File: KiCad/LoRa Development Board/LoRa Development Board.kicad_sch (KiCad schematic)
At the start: 0 parts

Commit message: Added SX1262 Symbol
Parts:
- added U1: ~, symbol Wireless Sensors:SX1262
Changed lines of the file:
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@@
     (company "NSE Labs")
+  )
+  (symbol (lib_id "Wireless Sensors:SX1262") (at 134.62 90.17 0) (unit 1)
+    (in_bom yes) (on_board yes) (dnp no) (fields_autoplaced)
+    (property "Reference" "U1" (at 137.8459 113.03 0)
+      (effects (font (size 1.27 1.27)) (justify left))
+    )
+    (property "Value" "~" (at 134.62 90.17 0)
+      (effects (font (size 1.27 1.27)))
+    )
+    (property "Footprint" "" (at 134.62 90.17 0)
+      (effects (font (size 1.27 1.27)) hide)
+    )
+    (property "Datasheet" "" (at 134.62 90.17 0)
+      (effects (font (size 1.27 1.27)) hide)
+    )
+    (pin "1")
+    (pin "10")
+    (pin "11")
+    (pin "12")
+    (pin "13")
+    (pin "14")
+    (pin "15")
+    (pin "16")
+    (pin "17")
+    (pin "18")
+    (pin "19")
+    (pin "2")
+    (pin "20")
+    (pin "21")
+    (pin "22")
+    (pin "23")
+    (pin "24")
+    (pin "3")
+    (pin "4")
+    (pin "5")
+    (pin "6")
+    (pin "7")
+    (pin "8")
+    (pin "9")
+    (instances
+      (project "LoRa Development Board"
+        (path "/81d1aadf-85d2-4fd0-839e-05ac66879581"
+          (reference "U1") (unit 1)
+        )
+      )
+    )
   )
   (sheet_instances

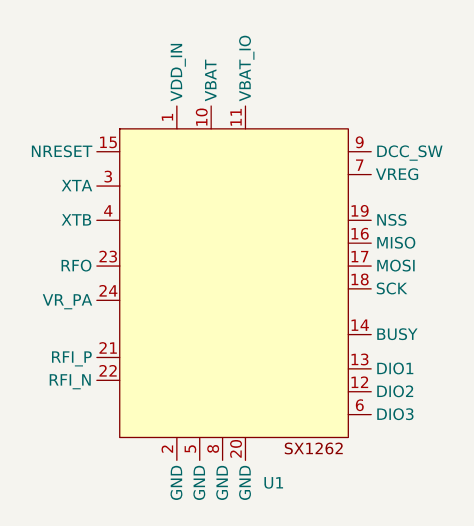
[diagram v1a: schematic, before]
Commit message: Update SX1262 Symbol
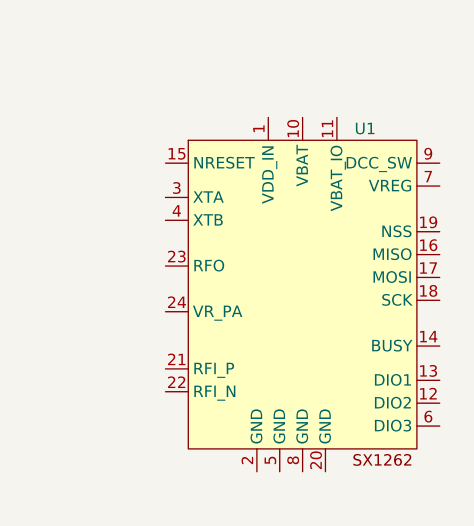
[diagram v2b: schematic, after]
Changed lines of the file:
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@@
     (company "NSE Labs")
   )
-  (symbol (lib_id "Wireless Sensors:SX1262") (at 134.62 90.17 0) (unit 1)
+  (symbol (lib_id "Wireless Sensors:SX1262") (at 142.24 91.44 0) (unit 1)
     (in_bom yes) (on_board yes) (dnp no) (fields_autoplaced)
-    (property "Reference" "U1" (at 137.8459 113.03 0)
+    (property "Reference" "U1" (at 148.0059 73.66 0)
       (effects (font (size 1.27 1.27)) (justify left))
     )
-    (property "Value" "~" (at 134.62 90.17 0)
+    (property "Value" "~" (at 142.24 91.44 0)
       (effects (font (size 1.27 1.27)))
     )
-    (property "Footprint" "" (at 134.62 90.17 0)
+    (property "Footprint" "" (at 142.24 91.44 0)
       (effects (font (size 1.27 1.27)) hide)
     )
-    (property "Datasheet" "" (at 134.62 90.17 0)
+    (property "Datasheet" "" (at 142.24 91.44 0)
       (effects (font (size 1.27 1.27)) hide)
     )

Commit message: Update LoRa Board Schematic
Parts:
- added C16: 1 uF, symbol Device:C_Small
- added C17: 470 nF, symbol Device:C_Small
- added C18: 100 nF, symbol Device:C_Small
- added L7: 15 uH, symbol Device:L_Small
- added Y1: 32.0 MHz, symbol Device:Crystal_GND24_Small
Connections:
- net +3.3V: now reaches U1.1 (VDD_IN)
- net +3.3V: now also U1.10 (VBAT), U1.11 (VBAT_IO), C16.2, C18.1
- net GND: now reaches U1.2 (GND)
- net GND: now also U1.20 (GND), U1.25 (GND), U1.5 (GND), U1.8 (GND), C16.1, C17.2, C18.2, Y1.2, Y1.4
- net at U1.3 (XTA): now also Y1.3
- net at U1.4 (XTB): now also Y1.1
- net at U1.7 (VREG): now also C17.1, L7.2
- net at U1.9 (DCC_SW): now also L7.1

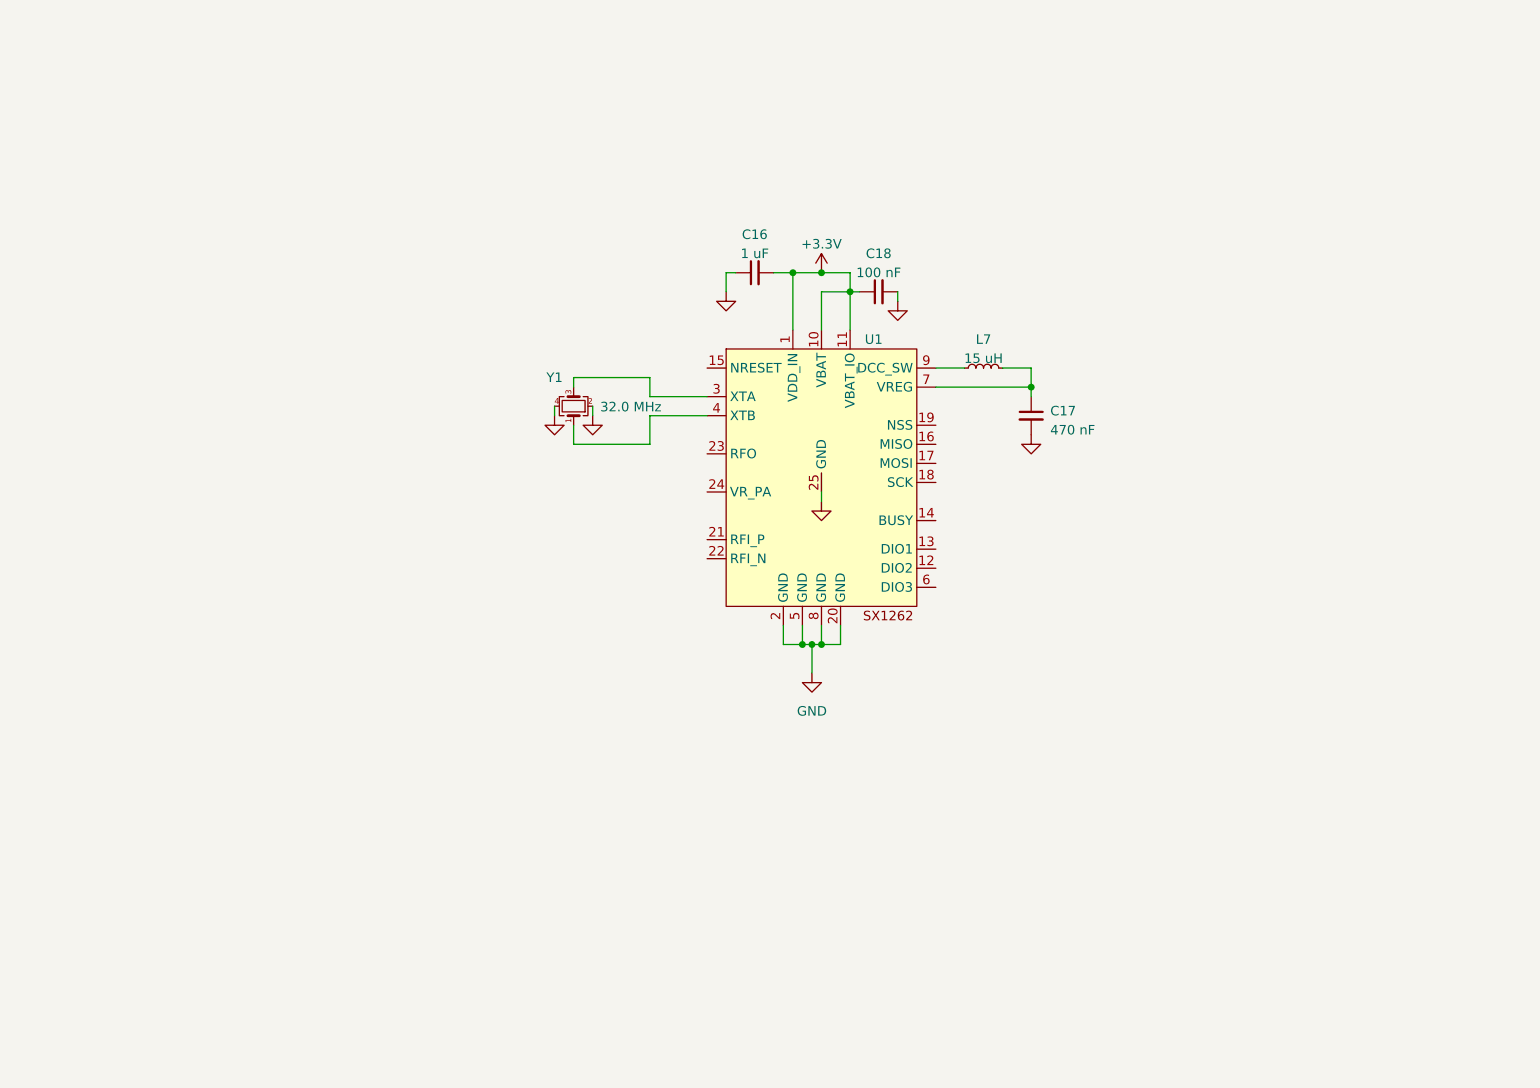
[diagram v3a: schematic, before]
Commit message: Completed schematic for LoRa board
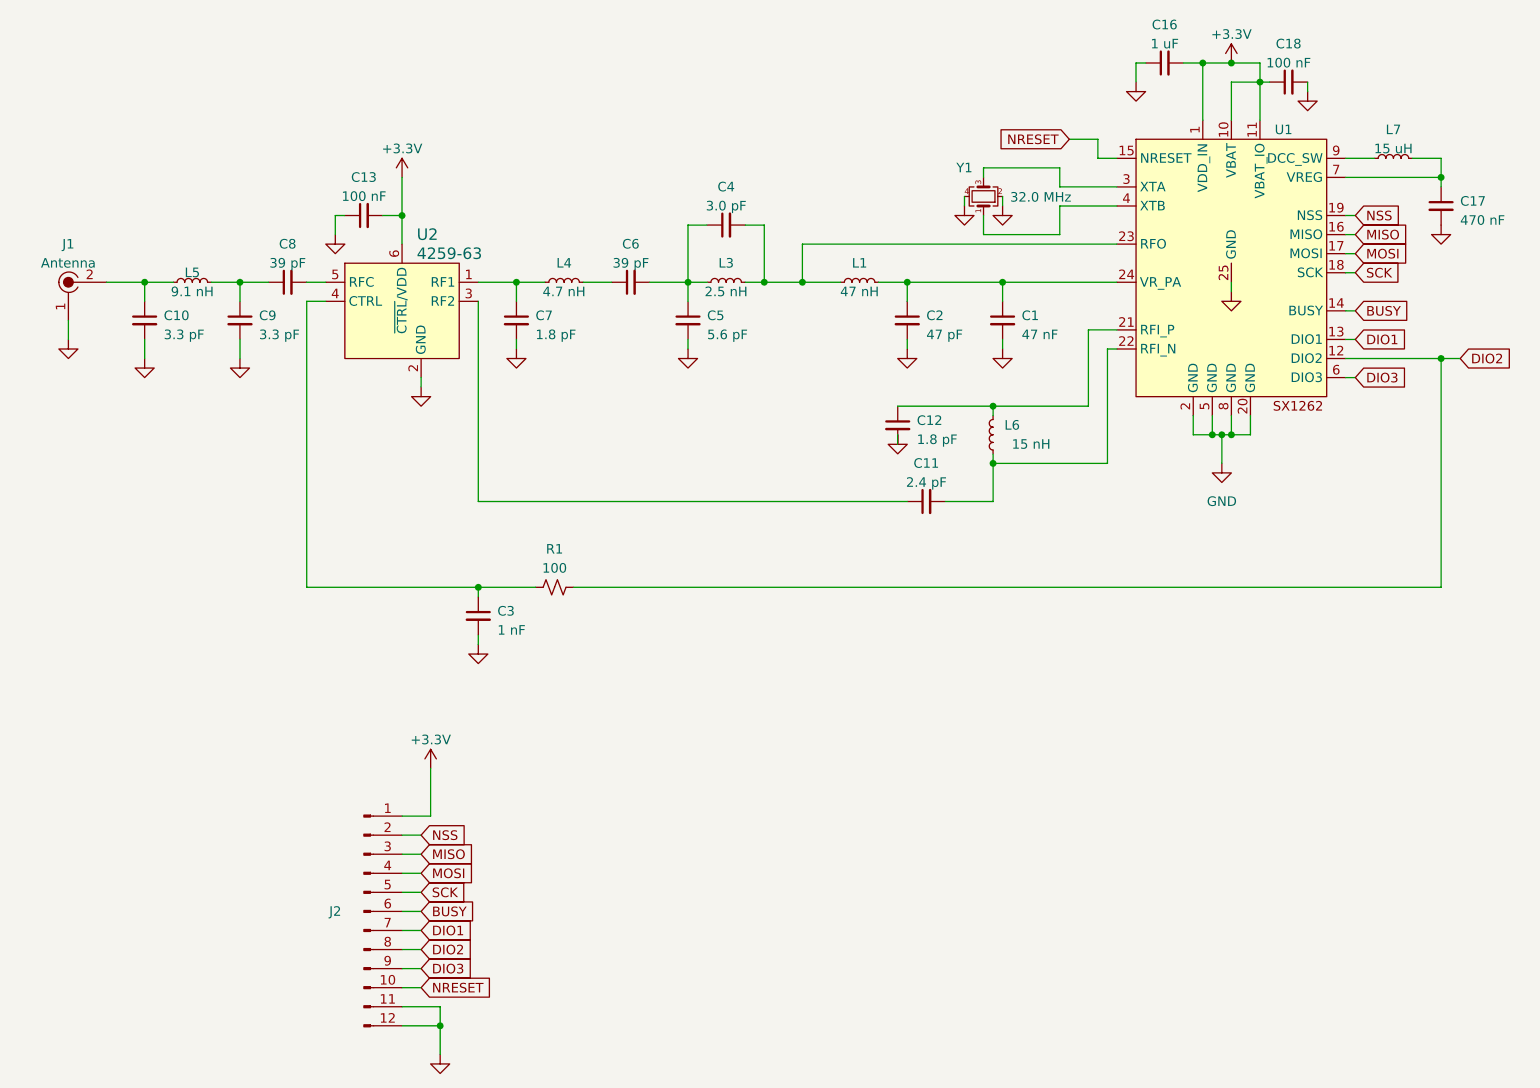
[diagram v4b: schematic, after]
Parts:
- added C1: 47 nF, symbol Device:C_Small
- added C10, C9: 3.3 pF, symbol Device:C_Small
- added C11: 2.4 pF, symbol Device:C_Small
- added C12, C7: 1.8 pF, symbol Device:C_Small
- added C13: 100 nF, symbol Device:C_Small
- added C2: 47 pF, symbol Device:C_Small
- added C3: 1 nF, symbol Device:C_Small
- added C4: 3.0 pF, symbol Device:C_Small
- added C5: 5.6 pF, symbol Device:C_Small
- added C6, C8: 39 pF, symbol Device:C_Small
- added J1: Antenna, digikey-footprints:Coax_Conn_U.FL, symbol dk_Coaxial-Connectors-RF:U_FL-R-SMT_10_
- added J2: ~, symbol Connector:Conn_01x12_Pin
- added L1: 47 nH, symbol Device:L_Small
- added L3: 2.5 nH, symbol Device:L_Small
- added L4: 4.7 nH, symbol Device:L_Small
- added L5: 9.1 nH, symbol Device:L_Small
- added L6: 15 nH, symbol Device:L_Small
- added R1: 100, symbol Device:R_Small_US
- added U2: 4259-63, digikey-footprints:SOT-363, symbol dk_RF-Switches:4259-63
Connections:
- net +3.3V: now also C13.2, J2.1 (Pin_1), U2.6 (~{CTRL}/VDD)
- net GND: now also C1.2, C10.2, C12.2, C13.1, C2.2, C3.2, C5.2, C7.2, C9.2, J1.1, J2.11 (Pin_11), J2.12 (Pin_12), U2.2 (GND)
- net DIO2: now reaches U1.12 (DIO2)
- net DIO2: now also J2.8 (Pin_8), R1.2
- net DIO1: now reaches U1.13 (DIO1)
- net DIO1: now also J2.7 (Pin_7)
- net BUSY: now reaches U1.14 (BUSY)
- net BUSY: now also J2.6 (Pin_6)
- net NRESET: now reaches U1.15 (NRESET)
- net NRESET: now also J2.10 (Pin_10)
- net MISO: now reaches U1.16 (MISO)
- net MISO: now also J2.3 (Pin_3)
- net MOSI: now reaches U1.17 (MOSI)
- net MOSI: now also J2.4 (Pin_4)
- net SCK: now reaches U1.18 (SCK)
- net SCK: now also J2.5 (Pin_5)
- net NSS: now reaches U1.19 (NSS)
- net NSS: now also J2.2 (Pin_2)
- net at U1.21 (RFI_P): now also C12.1, L6.2
- net at U1.22 (RFI_N): now also C11.2, L6.1
- net at U1.23 (RFO): now also C4.2, L1.1, L3.2
- net at U1.24 (VR_PA): now also C1.1, C2.1, L1.2
- net DIO3: now reaches U1.6 (DIO3)
- net DIO3: now also J2.9 (Pin_9)
- new net: C4.1, C5.1, C6.2, L3.1
- new net: C10.1, J1.2, L5.1
- new net: C8.1, C9.1, L5.2
- new net: C7.1, L4.1, U2.1 (RF1)
- new net: C11.1, U2.3 (RF2)
- new net: C6.1, L4.2
- new net: C3.1, R1.1, U2.4 (CTRL)
- new net: C8.2, U2.5 (RFC)
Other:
- moved on the sheet: C16, C17, C18, L7, U1, Y1

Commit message: Completed design and BOM
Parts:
- added R2: 100, symbol Device:R_Small_US
- C13: value 100 nF -> 1 nF
- renumbered C16 to C14, C18 to C15, C17 to C16
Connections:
- net +3.3V: no longer C13.2, U2.6 (~{CTRL}/VDD)
- net GND: no longer J2.11 (Pin_11)
- new net: C13.2, R2.1, U2.6 (~{CTRL}/VDD)
- new net ANT_SW: J2.11 (Pin_11), R2.2
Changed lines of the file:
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@@
   (title_block
     (title "LoRa Development Board")
-    (date "2023-05-02")
+    (date "2023-05-03")
     (rev "1")
     (company "NSE Labs")
@@
   (junction (at 96.52 106.68) (diameter 0) (color 0 0 0 0)
   )
-  (junction (at 91.44 165.1) (diameter 0) (color 0 0 0 0)
-  )
   (junction (at 194.31 86.36) (diameter 0) (color 0 0 0 0)
   )
@@
     (stroke (width 0) (type default))
   )
-  (wire (pts (xy 86.36 162.56) (xy 91.44 162.56))
-    (stroke (width 0) (type default))
-  )
   (wire (pts (xy 86.36 144.78) (xy 88.9 144.78))
     (stroke (width 0) (type default))
@@
     (stroke (width 0) (type default))
   )
-  (wire (pts (xy 86.36 52.07) (xy 86.36 57.15))
+  (wire (pts (xy 86.36 46.99) (xy 86.36 57.15))
     (stroke (width 0) (type default))
   )
@@
     (stroke (width 0) (type default))
   )
+  (wire (pts (xy 96.52 46.99) (xy 101.6 46.99))
+    (stroke (width 0) (type default))
+  )
   (wire (pts (xy 227.33 76.2) (xy 224.79 76.2))
     (stroke (width 0) (type default))
@@
     (stroke (width 0) (type default))
   )
+  (wire (pts (xy 86.36 162.56) (xy 88.9 162.56))
+    (stroke (width 0) (type default))
+  )
   (wire (pts (xy 200.66 39.37) (xy 201.93 39.37))
     (stroke (width 0) (type default))
@@
     (stroke (width 0) (type default))
   )
+  (wire (pts (xy 91.44 46.99) (xy 86.36 46.99))
+    (stroke (width 0) (type default))
+  )
   (wire (pts (xy 64.77 73.66) (xy 64.77 76.2))
     (stroke (width 0) (type default))
@@
   )
   (wire (pts (xy 181.61 74.93) (xy 180.34 74.93))
-    (stroke (width 0) (type default))
-  )
-  (wire (pts (xy 91.44 162.56) (xy 91.44 165.1))
     (stroke (width 0) (type default))
   )
@@
     )
   )
+  (global_label "ANT_SW" (shape input) (at 88.9 162.56 0) (fields_autoplaced)
+    (effects (font (size 1.27 1.27)) (justify left))
+    (property "Intersheetrefs" "${INTERSHEET_REFS}" (at 98.821 162.56 0)
+      (effects (font (size 1.27 1.27)) (justify left) hide)
+    )
+  )
   (global_label "BUSY" (shape input) (at 88.9 149.86 0) (fields_autoplaced)
     (effects (font (size 1.27 1.27)) (justify left))
@@
     )
   )
+  (global_label "ANT_SW" (shape input) (at 101.6 46.99 0) (fields_autoplaced)
+    (effects (font (size 1.27 1.27)) (justify left))
+    (property "Intersheetrefs" "${INTERSHEET_REFS}" (at 111.521 46.99 0)
+      (effects (font (size 1.27 1.27)) (justify left) hide)
+    )
+  )
   (global_label "DIO2" (shape input) (at 88.9 154.94 0) (fields_autoplaced)
     (effects (font (size 1.27 1.27)) (justify left))
@@
   (symbol (lib_id "Device:C_Small") (at 204.47 39.37 90) (unit 1)
     (in_bom yes) (on_board yes) (dnp no) (fields_autoplaced)
-    (property "Reference" "C18" (at 204.4763 34.29 90)
+    (property "Reference" "C15" (at 204.4763 34.29 90)
       (effects (font (size 1.27 1.27)))
     )
@@
       (project "LoRa Development Board"
         (path "/81d1aadf-85d2-4fd0-839e-05ac66879581"
-          (reference "C18") (unit 1)
+          (reference "C15") (unit 1)
         )
       )
@@
         (path "/81d1aadf-85d2-4fd0-839e-05ac66879581"
           (reference "#PWR01") (unit 1)
-        )
-      )
-    )
-  )
-  (symbol (lib_id "power:+3.3V") (at 86.36 52.07 0) (unit 1)
-    (in_bom yes) (on_board yes) (dnp no) (fields_autoplaced)
-    (property "Reference" "#PWR019" (at 86.36 55.88 0)
-      (effects (font (size 1.27 1.27)) hide)
-    )
-    (property "Value" "+3.3V" (at 86.36 48.26 0)
-      (effects (font (size 1.27 1.27)))
-    )
-    (property "Footprint" "" (at 86.36 52.07 0)
-      (effects (font (size 1.27 1.27)) hide)
-    )
-    (property "Datasheet" "" (at 86.36 52.07 0)
-      (effects (font (size 1.27 1.27)) hide)
-    )
-    (pin "1")
-    (instances
-      (project "LoRa Development Board"
-        (path "/81d1aadf-85d2-4fd0-839e-05ac66879581"
-          (reference "#PWR019") (unit 1)
         )
       )
@@
       (effects (font (size 1.27 1.27)))
     )
-    (property "Value" "100 nF" (at 81.2863 54.61 90)
+    (property "Value" "1 nF" (at 81.2863 54.61 90)
       (effects (font (size 1.27 1.27)))
     )
@@
     )
   )
+  (symbol (lib_id "Device:R_Small_US") (at 93.98 46.99 90) (unit 1)
+    (in_bom yes) (on_board yes) (dnp no) (fields_autoplaced)
+    (property "Reference" "R2" (at 93.98 41.91 90)
+      (effects (font (size 1.27 1.27)))
+    )
+    (property "Value" "100" (at 93.98 44.45 90)
+      (effects (font (size 1.27 1.27)))
+    )
+    (property "Footprint" "" (at 93.98 46.99 0)
+      (effects (font (size 1.27 1.27)) hide)
+    )
+    (property "Datasheet" "~" (at 93.98 46.99 0)
+      (effects (font (size 1.27 1.27)) hide)
+    )
+    (pin "1")
+    (pin "2")
+    (instances
+      (project "LoRa Development Board"
+        (path "/81d1aadf-85d2-4fd0-839e-05ac66879581"
+          (reference "R2") (unit 1)
+        )
+      )
+    )
+  )
   (symbol (lib_id "Device:C_Small") (at 224.79 55.88 0) (unit 1)
     (in_bom yes) (on_board yes) (dnp no) (fields_autoplaced)
-    (property "Reference" "C17" (at 227.33 55.2513 0)
+    (property "Reference" "C16" (at 227.33 55.2513 0)
       (effects (font (size 1.27 1.27)) (justify left))
     )
@@
       (project "LoRa Development Board"
         (path "/81d1aadf-85d2-4fd0-839e-05ac66879581"
-          (reference "C17") (unit 1)
+          (reference "C16") (unit 1)
         )
       )
@@
   (symbol (lib_id "Device:C_Small") (at 187.96 36.83 90) (unit 1)
     (in_bom yes) (on_board yes) (dnp no) (fields_autoplaced)
-    (property "Reference" "C16" (at 187.9663 31.75 90)
+    (property "Reference" "C14" (at 187.9663 31.75 90)
       (effects (font (size 1.27 1.27)))
     )
@@
       (project "LoRa Development Board"
         (path "/81d1aadf-85d2-4fd0-839e-05ac66879581"
-          (reference "C16") (unit 1)
-        )
-      )
+          (reference "C14") (unit 1)
+        )
+      )

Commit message: Changed RF switch on LoRa board
Based on parts availability
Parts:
- removed R2: 100, symbol Device:R_Small_US
- removed U2: 4259-63, digikey-footprints:SOT-363, symbol dk_RF-Switches:4259-63
- added U3: ~, symbol Wireless Sensors:HMC8038
- C13: value 1 nF -> 100 nF
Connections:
- net ANT_SW is gone; now on net GND: J2.11 (Pin_11)
- net +3.3V: now also C13.1, U3.1 (VDD)
- net GND: now also C13.2, U3.10 (GND), U3.11 (GND), U3.5 (EN); no longer C13.1
- net at C7.1, L4.1: now also U3.9 (RF1)
- net at C11.1: now also U3.12 (RF2)
- net at C3.1, R1.1: now also U3.2 (VCTL)
- net at C8.2: now also U3.3 (RFC)
- no-connect marks 0 -> 7
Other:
- moved on the sheet: C10, C3, C8, C9, J1, L5, R1
